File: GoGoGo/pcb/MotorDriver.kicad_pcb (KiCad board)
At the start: 2 copper layers, 9 parts, among them P101 CONN_01X02, P102 CONN_01X04, P103 CONN_01X02, P104 CONN_01X02, U101 TB6593FNG

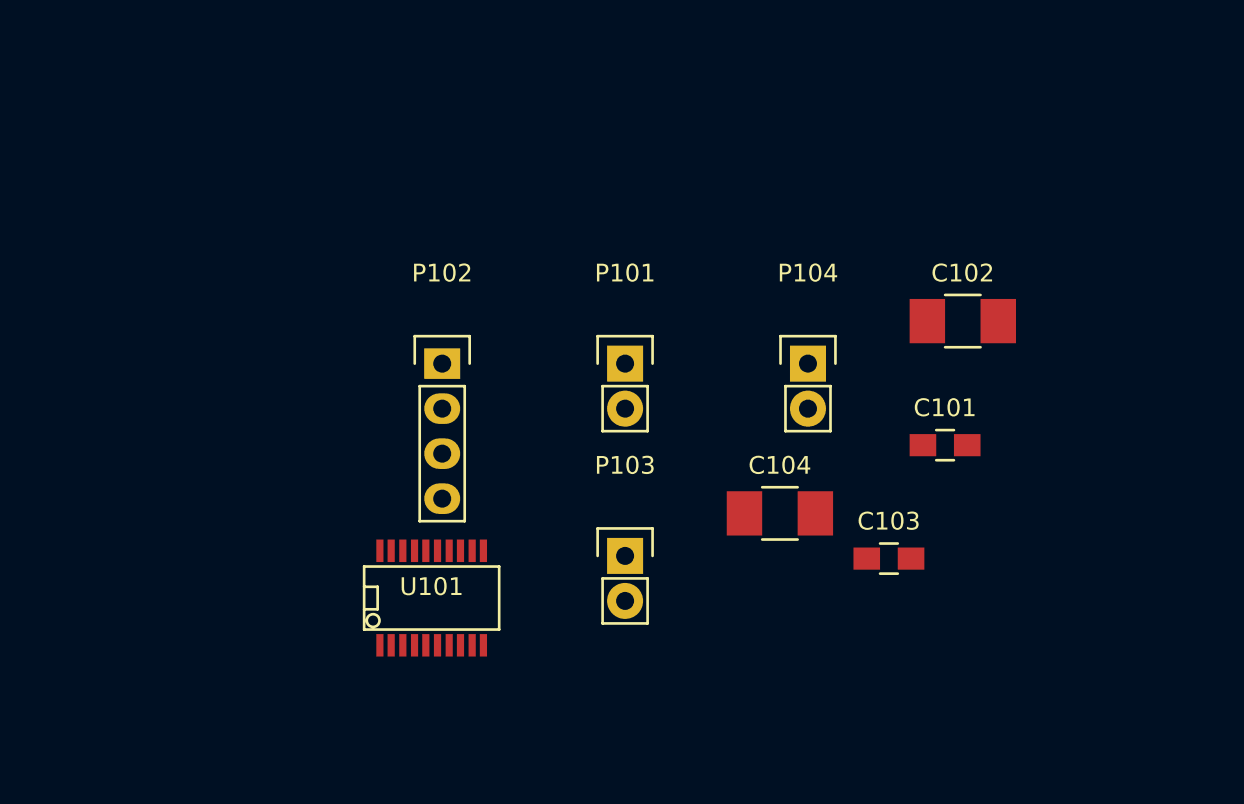
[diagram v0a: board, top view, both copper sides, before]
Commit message: MotorDriver pcb rough layout
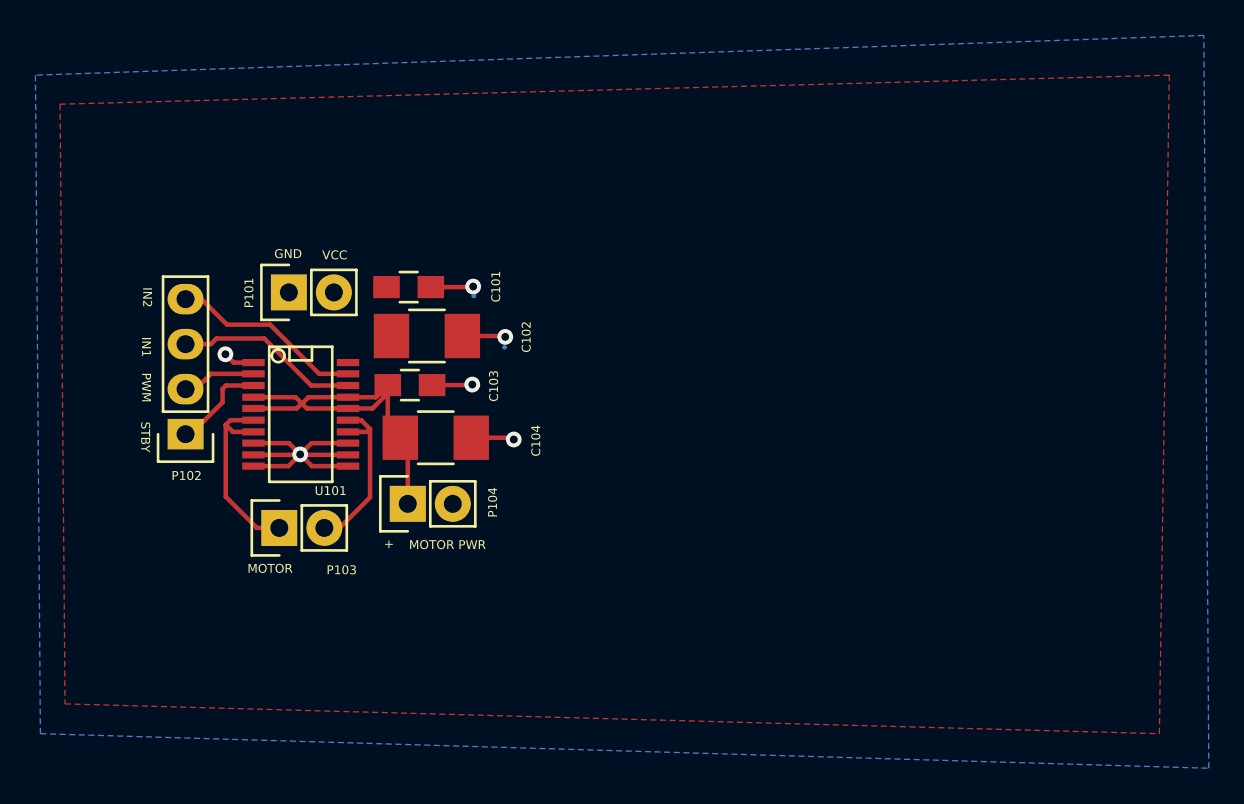
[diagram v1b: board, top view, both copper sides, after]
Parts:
- moved C101 31.6 mm to (144.0, 99.2)
- moved C102 30.3 mm to (145.0, 102.0)
- moved C103 28.7 mm to (144.1, 104.8)
- moved P104 23.9 mm to (143.9, 111.5), turned to 90 degrees
- moved C104 19.9 mm to (145.5, 107.7)
- moved P103 19.6 mm to (136.7, 112.8), turned to 90 degrees
- moved P101 19.4 mm to (137.2, 99.5), turned to 90 degrees
- moved P102 15.0 mm to (131.4, 107.5), turned to 180 degrees
- moved U101 12.7 mm to (137.9, 106.4), turned to 270 degrees
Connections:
- P102 pad 1: /PWM -> /STBY
- P102 pad 2: /IN2 -> /PWM
- P102 pad 4: /STBY -> /IN2
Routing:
- net GND: track 0.00 -> 28.4 mm, vias 0 -> 6
- net /PM+: track 0.00 -> 25.3 mm
- net /M+: track 0.00 -> 11.2 mm
- net /IN2: track 0.00 -> 10.9 mm
- net /IN1: track 0.00 -> 10.4 mm
- net Net-(P103-Pad2): track 0.00 -> 9.91 mm
- net /STBY: track 0.00 -> 5.42 mm
- net /PWM: track 0.00 -> 4.19 mm
- added copper zone on B.Cu, net GND
- added copper zone on F.Cu, net Net-(C101-Pad1)
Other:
- board text added: "+"
- board text added: "GND"
- board text added: "IN1"
- board text added: "IN2"
- board text added: "MOTOR"
- board text added: "MOTOR PWR"
- board text added: "PWM"
- board text added: "STBY"
- board text added: "VCC"

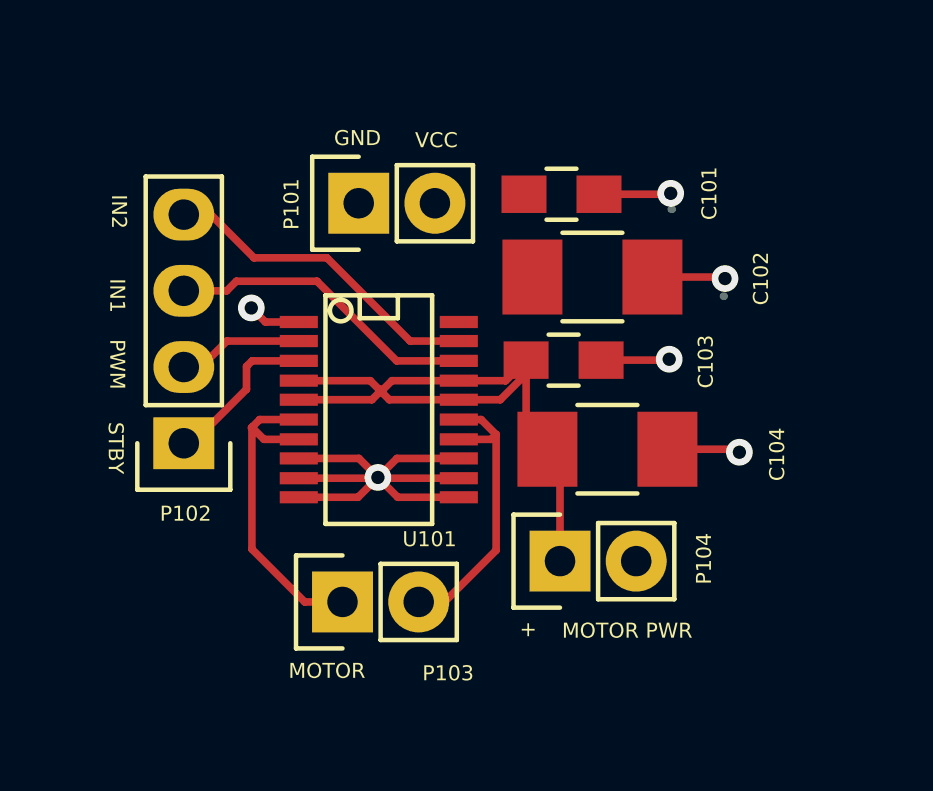
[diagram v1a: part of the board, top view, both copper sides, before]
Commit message: Increased GGG MotorDriver track widths
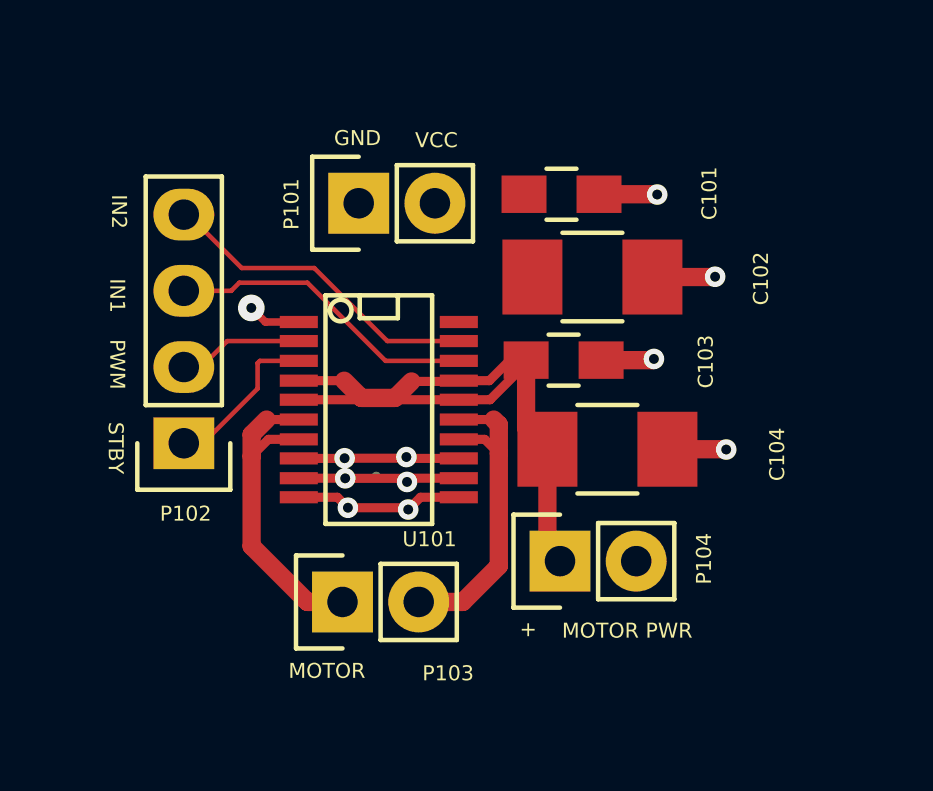
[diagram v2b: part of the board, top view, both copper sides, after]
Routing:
- net GND: track 28.4 -> 26.1 mm, vias 6 -> 11
- net Net-(P103-Pad2): track 9.91 -> 11.7 mm
- net /IN2: track 10.9 -> 11.8 mm
- net /PWM: track 4.19 -> 4.76 mm
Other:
- net class Default: clearance 0.254 -> 0.1524; trace_width 0.254 -> 0.1524; via_dia 0.889 -> 0.6858; via_drill 0.635 -> 0.3302
- rule trace_clearance: 0.254 -> 0.1524
- rule trace_min: 0.254 -> 0.1524
- rule via_min_drill: 0.508 -> 0.3302
- rule via_min_size: 0.889 -> 0.6858

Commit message: Created gerbers for GGG Motor Driver
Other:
- board outline added: 21.5 x 18.8 mm
- board text added: "GGG Motor Driver v1"
- board text added: "License: CCBY"
- board text added: "brooke.t.hedrick@gmail.com"
- board text added: "github hedrickbt/ContextualElectronics/... tree/master/GoGoGo/pcb"
